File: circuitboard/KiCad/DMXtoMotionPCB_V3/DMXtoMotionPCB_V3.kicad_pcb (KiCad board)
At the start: 2 copper layers, 93.8 x 100 mm, 55 parts, among them J1 12V In, J10 D2, J2 XLR3 IN, J3 XLR3 OUT, J4 D1, J5 INTERFACE, J6 A0, J7 A1, J8 D0, J9 D3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

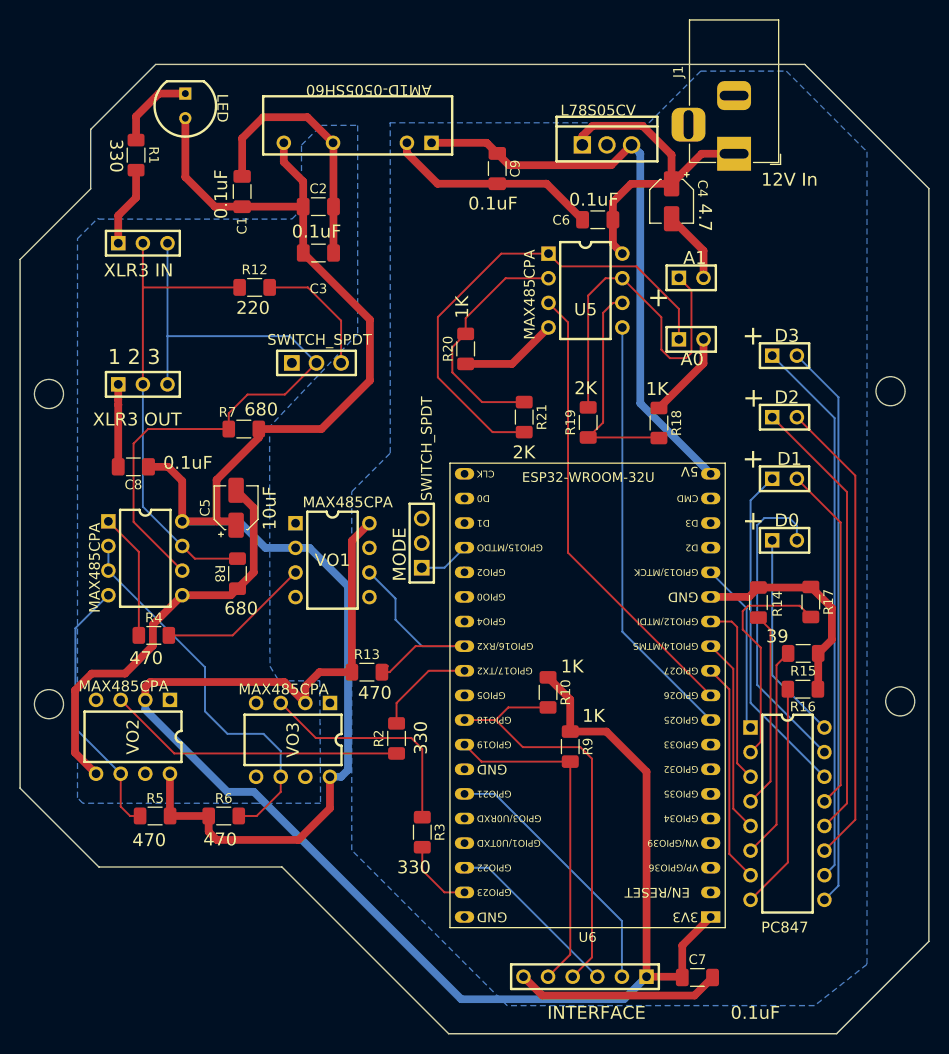
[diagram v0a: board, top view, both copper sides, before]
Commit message: Slight modifications on KiCAD V3 files. Generated fabrication files
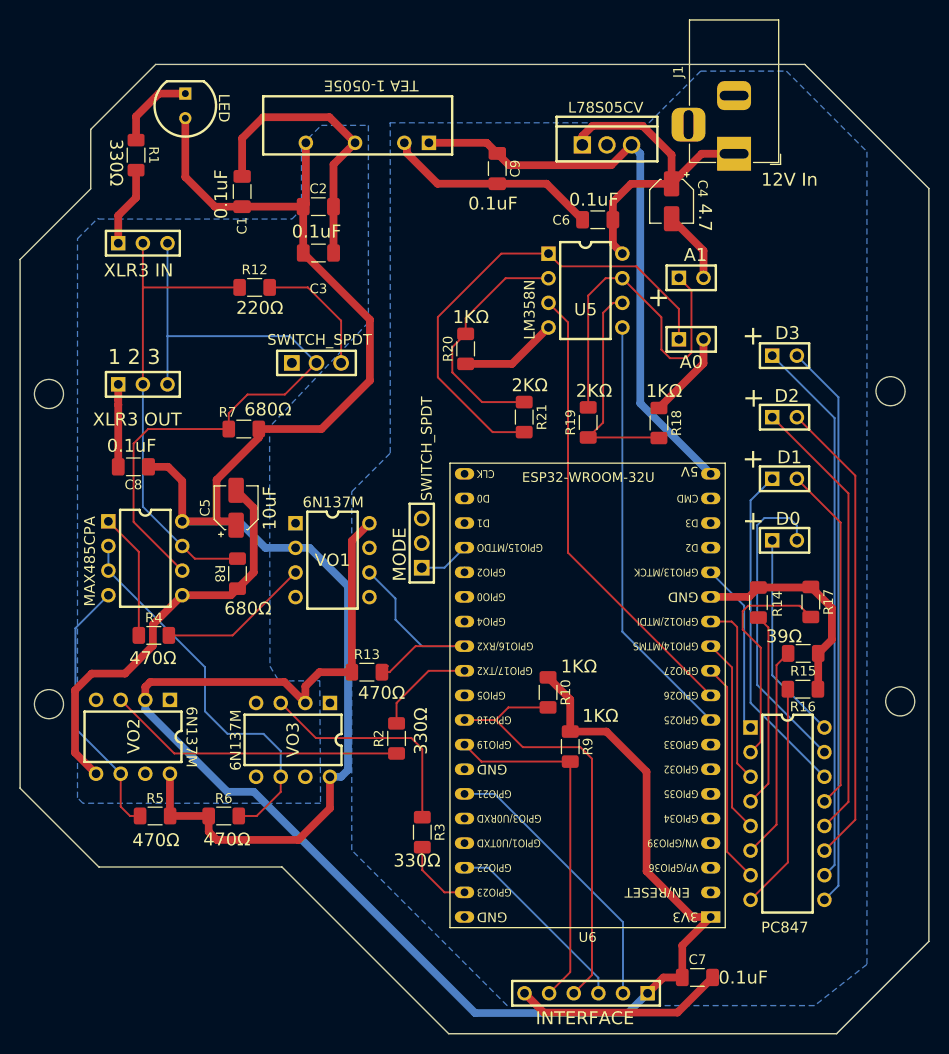
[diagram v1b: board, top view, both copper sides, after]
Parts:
- moved J5 1.71 mm to (158.4, 150.8)
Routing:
- net ISO-GND: track 87.4 -> 90.2 mm
- net Net_33: track 18.4 -> 20.1 mm
- net Net_32: track 27.4 -> 29.2 mm
- net But1: track 44.1 -> 45.7 mm
- net But2: track 35.2 -> 36.9 mm
- net 3.3V_ESP: track 156.7 -> 155.6 mm
- net ISO-5V: track 154.4 -> 153.7 mm
- net GND: track 92.5 -> 93.1 mm
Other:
- board text added: "1KΩ"
- board text added: "220Ω"
- board text added: "2KΩ"
- board text added: "330Ω"
- board text added: "39Ω"
- board text added: "470Ω"
- board text added: "680Ω"
- board text removed: "1K"
- board text removed: "220"
- board text removed: "2K"
- board text removed: "330"
- board text removed: "39"
- board text removed: "470"
- board text removed: "680"

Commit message: Changes of through hole diameters in KiCAD V3 and BOM
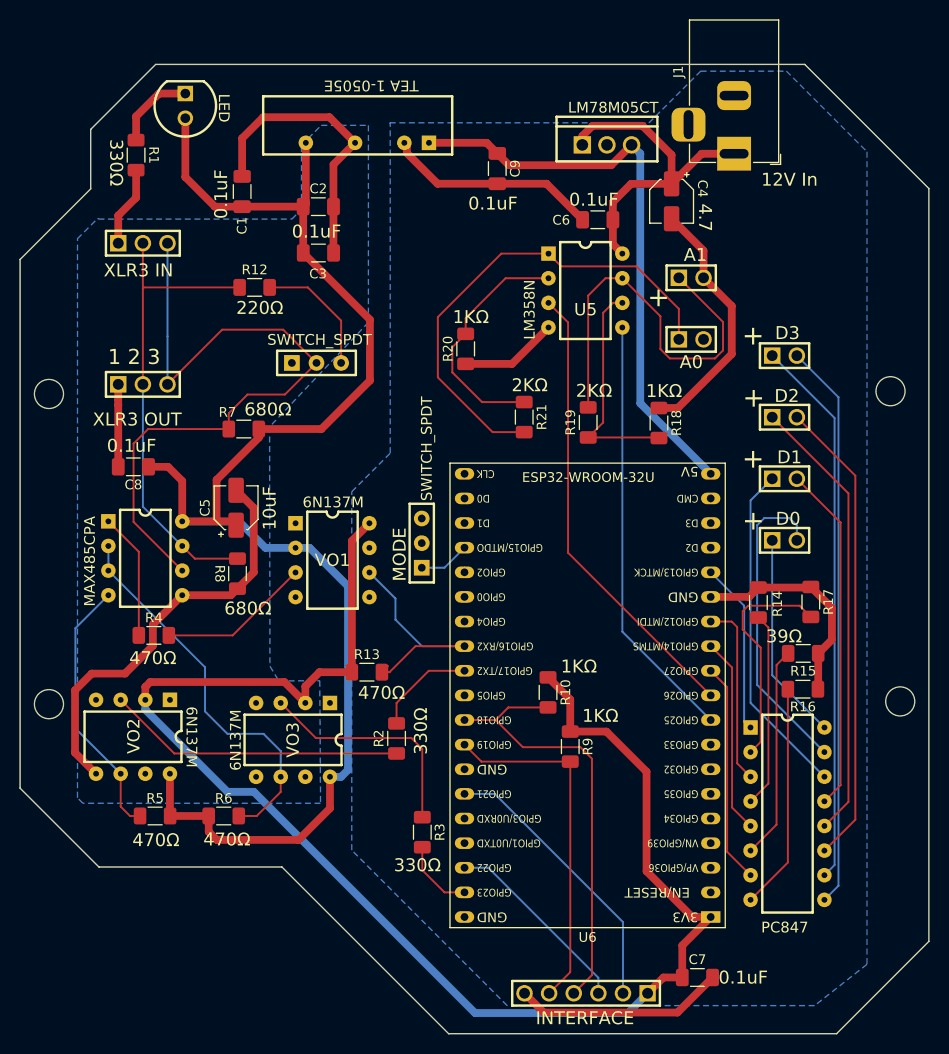
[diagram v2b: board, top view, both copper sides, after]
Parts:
- U4: value L78S05CV -> LM78M05CT
- VO2, VO3: value 6N137M_10 -> 6N137M
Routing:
- net GND: track 93.1 -> 103.0 mm
- net Net_18: track 36.8 -> 41.6 mm
- net Net_17: track 69.5 -> 72.1 mm

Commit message: Actualización de componentes obsoletos
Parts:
- U4: value LM78M05CT -> L78S05CV
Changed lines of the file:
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@@
 			)
 		)
-		(property "Value" "LM78M05CT"
+		(property "Value" "L78S05CV "
 			(at 0 0 0)
 			(layer "F.Fab")
@@
 			(layer "F.SilkS")
 		)
-		(fp_text user "LM78M05CT"
+		(fp_text user "L78S05CV "
 			(at -4.0261 -3.1961 0)
 			(unlocked yes)

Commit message: double checked through holes and part names. Completed BOM
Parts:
- U1: value AM1D-0505SH60 -> TEA 1-0505E
- VO1, VO2, VO3: value 6N137M -> 6N137
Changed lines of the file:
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@@
 			)
 		)
-		(property "Value" "6N137M"
+		(property "Value" "6N137"
 			(at 0 0 0)
 			(layer "F.Fab")
@@
 			(layer "F.SilkS")
 		)
-		(fp_text user "6N137M"
+		(fp_text user "6N137"
 			(at -3.1411 -5.3889 -90)
 			(unlocked yes)
@@
 		)
 		(fp_line
-			(start 0.9 1.9)
+			(start 0.9 2.2352)
 			(end 0.9 4.6)
 			(stroke
@@
 		(fp_line
 			(start 0.9 -4.6)
-			(end 0.9 -2)
+			(end 0.9 -2.2352)
 			(stroke
 				(width 0.12)
@@
 		(pad "1" thru_hole rect
 			(at 0 0 270)
-			(size 3.5 3.5)
-			(drill oval 1 3)
+			(size 3.5 4)
+			(drill oval 1 3.5)
 			(layers "*.Cu" "*.Mask")
 			(remove_unused_layers no)
@@
 		(pad "1" thru_hole rect
 			(at -2.54 0 90)
-			(size 1.62 1.62)
-			(drill 0.8)
+			(size 1.92 1.92)
+			(drill 1.1)
 			(layers "*.Cu" "*.Mask")
 			(remove_unused_layers no)
@@
 		(pad "2" thru_hole circle
 			(at 0 0 90)
-			(size 1.62 1.62)
-			(drill 0.8)
+			(size 1.92 1.92)
+			(drill 1.1)
 			(layers "*.Cu" "*.Mask")
 			(remove_unused_layers no)
@@
 		(pad "3" thru_hole circle
 			(at 2.54 0 90)
-			(size 1.62 1.62)
-			(drill 0.8)
+			(size 1.92 1.92)
+			(drill 1.1)
 			(layers "*.Cu" "*.Mask")
 			(remove_unused_layers no)
@@
 			)
 		)
-		(property "Value" "AM1D-0505SH60"
+		(property "Value" "TEA 1-0505E"
 			(at 0 0 180)
 			(layer "F.Fab")
@@
 			)
 		)
-		(property "Value" "6N137M"
+		(property "Value" "6N137"
 			(at -0.07 0.1 90)
 			(layer "F.Fab")
@@
 			(layer "F.SilkS")
 		)
-		(fp_text user "6N137M"
+		(fp_text user "6N137"
 			(at -3.09 -5.32 0)
 			(unlocked yes)
@@
 		(pad "1" thru_hole rect
 			(at -2.54 0)
-			(size 1.62 1.62)
-			(drill 0.8)
+			(size 1.92 1.92)
+			(drill 1.1)
 			(layers "*.Cu" "*.Mask")
 			(remove_unused_layers no)
@@
 		(pad "2" thru_hole circle
 			(at 0 0)
-			(size 1.62 1.62)
-			(drill 0.8)
+			(size 1.92 1.92)
+			(drill 1.1)
 			(layers "*.Cu" "*.Mask")
 			(remove_unused_layers no)
@@
 		(pad "3" thru_hole circle
 			(at 2.54 0)
-			(size 1.62 1.62)
-			(drill 0.8)
+			(size 1.92 1.92)
+			(drill 1.1)
 			(layers "*.Cu" "*.Mask")
 			(remove_unused_layers no)
@@
 			)
 		)
-		(property "Value" "6N137M"
+		(property "Value" "6N137"
 			(at 0.2414 -0.2489 0)
 			(layer "F.Fab")
@@
 			(layer "F.SilkS")
 		)
-		(fp_text user "6N137M"
+		(fp_text user "6N137"
 			(at 3.1914 5.2611 90)
 			(unlocked yes)

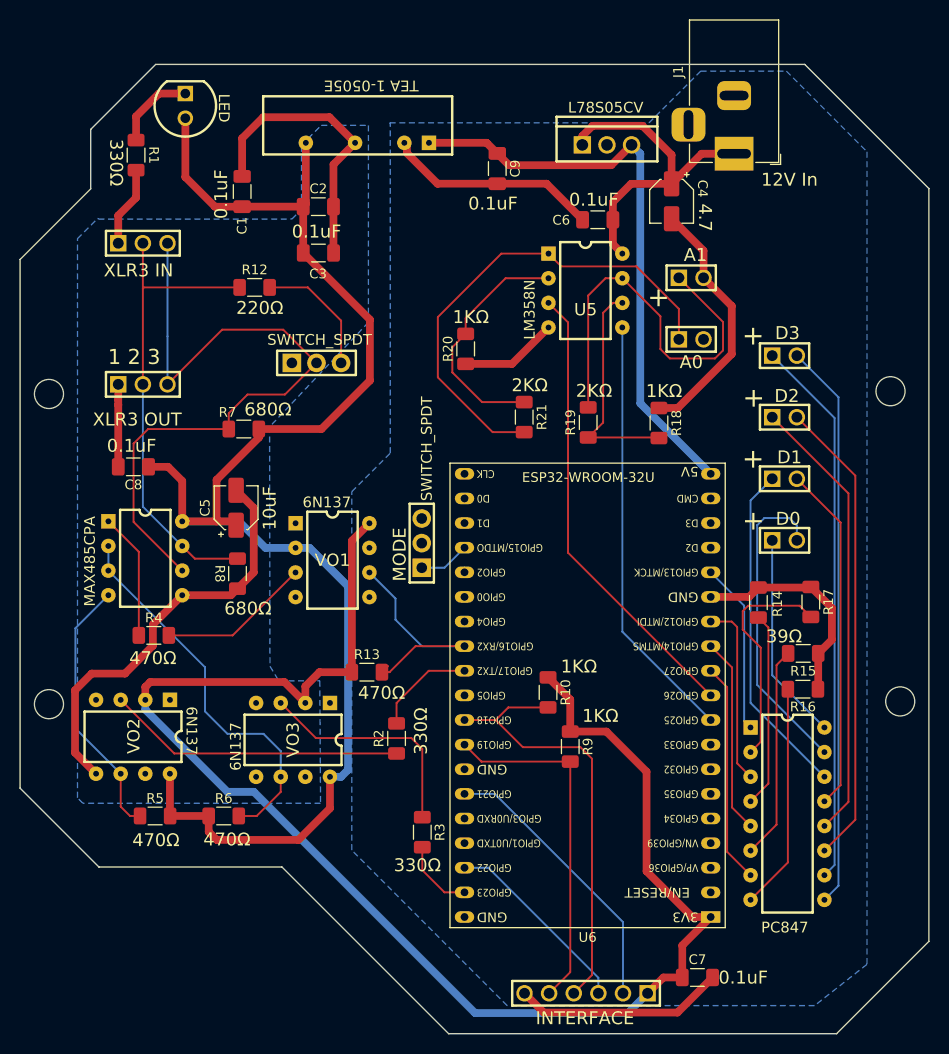
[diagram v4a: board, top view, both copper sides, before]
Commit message: trace adjustments
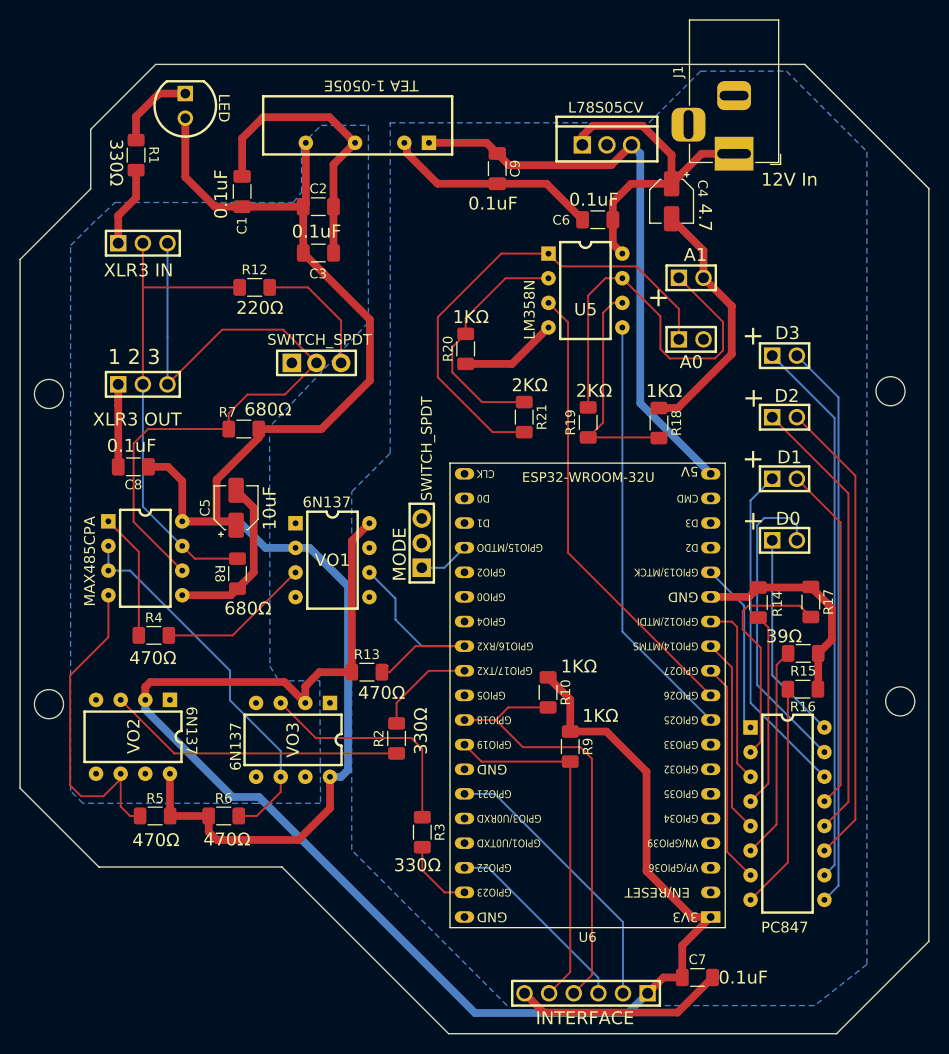
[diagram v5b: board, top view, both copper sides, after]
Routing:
- net ISO-GND: track 90.2 -> 64.3 mm
- net Net_15: track 27.5 -> 34.0 mm
- net Net_14: track 40.3 -> 39.4 mm
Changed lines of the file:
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@@
-	)
-	(segment
-		(start 124.1386 130.0486)
-		(end 146.96 152.87)
-		(width 0.8)
-		(layer "B.Cu")
-		(net 1)
-	)
-	(segment
-		(start 121.4186 130.0486)
-		(end 124.1386 130.0486)
-		(width 0.8)
-		(layer "B.Cu")
-		(net 1)
-	)
-	(segment
-		(start 112.9411 121.5711)
-		(end 121.4186 130.0486)
-		(width 0.8)
-		(layer "B.Cu")
-		(net 1)
 	)
 	(segment
@@
 	)
 	(segment
+		(start 121.95 130.58)
+		(end 124.67 130.58)
+		(width 0.8)
+		(layer "B.Cu")
+		(net 1)
+	)
+	(segment
+		(start 162.72 152.87)
+		(end 164.76 150.83)
+		(width 0.8)
+		(layer "B.Cu")
+		(net 1)
+	)
+	(segment
+		(start 124.67 130.58)
+		(end 146.96 152.87)
+		(width 0.8)
+		(layer "B.Cu")
+		(net 1)
+	)
+	(segment
+		(start 112.9411 121.5711)
+		(end 121.95 130.58)
+		(width 0.8)
+		(layer "B.Cu")
+		(net 1)
+	)
+	(segment
 		(start 146.96 152.87)
 		(end 162.72 152.87)
@@
 	)
 	(segment
-		(start 162.72 152.87)
-		(end 164.76 150.83)
-		(width 0.8)
-		(layer "B.Cu")
-		(net 1)
-	)
-	(segment
 		(start 150.4625 65.4)
 		(end 161.0122 65.4)
@@
 	)
 	(segment
-		(start 105.69 126.01)
-		(end 107.8611 128.1811)
-		(width 0.8)
-		(layer "F.Cu")
-		(net 7)
-	)
-	(segment
 		(start 110.15 73.45)
 		(end 110.15 70.59)
@@
 	)
 	(segment
-		(start 105.69 119.574141)
-		(end 105.69 126.01)
-		(width 0.8)
-		(layer "F.Cu")
-		(net 7)
-	)
-	(segment
 		(start 132.3525 69.68)
 		(end 132.3525 65.3237)
@@
 	)
 	(segment
-		(start 113.72 112.7972)
-		(end 113.72 114.976852)
-		(width 0.8)
-		(layer "F.Cu")
-		(net 7)
-	)
-	(segment
 		(start 132.3525 69.68)
 		(end 132.3525 74.45)
@@
 	)
 	(segment
-		(start 113.72 114.976852)
-		(end 110.846852 117.85)
-		(width 0.8)
-		(layer "F.Cu")
-		(net 7)
-	)
-	(segment
 		(start 124.12498 107.415048)
 		(end 122.450028 109.09)
@@
 	)
 	(segment
-		(start 116.7511 109.7661)
-		(end 113.72 112.7972)
-		(width 0.8)
-		(layer "F.Cu")
-		(net 7)
-	)
-	(segment
-		(start 107.414141 117.85)
-		(end 105.69 119.574141)
-		(width 0.8)
-		(layer "F.Cu")
-		(net 7)
-	)
-	(segment
-		(start 110.846852 117.85)
-		(end 107.414141 117.85)
-		(width 0.8)
-		(layer "F.Cu")
-		(net 7)
-	)
-	(segment
 		(start 110.15 70.59)
 		(end 111.98864 68.75136)
@@
 	)
 	(segment
-		(start 119.1 121.75)
-		(end 121.41 124.06)
+		(start 121.68 117.54)
+		(end 121.68 120.61)
 		(width 0.2)
 		(layer "B.Cu")
@@
 	)
 	(segment
-		(start 119.1 117.195)
-		(end 119.1 121.75)
+		(start 109.1311 107.2261)
+		(end 111.3661 107.2261)
 		(width 0.2)
 		(layer "B.Cu")
@@
 	)
 	(segment
-		(start 121.41 124.06)
-		(end 125.13 124.06)
-		(width 0.2)
-		(layer "B.Cu")
-		(net 44)
-	)
-	(segment
-		(start 109.1311 107.2261)
-		(end 119.1 117.195)
+		(start 121.68 120.61)
+		(end 126.9111 125.8411)
 		(width 0.2)
 		(layer "B.Cu")
@@
 	)
 	(segment
-		(start 125.13 124.06)
-		(end 126.9111 125.8411)
+		(start 111.3661 107.2261)
+		(end 121.68 117.54)
 		(width 0.2)
 		(layer "B.Cu")
@@
 	)
 	(segment
+		(start 105.18 118.04)
+		(end 105.18 129.37)
+		(width 0.2)
+		(layer "F.Cu")
+		(net 46)
+	)
+	(segment
+		(start 109.1311 114.0889)
+		(end 105.18 118.04)
+		(width 0.2)
+		(layer "F.Cu")
+		(net 46)
+	)
+	(segment
+		(start 108.62 130.5)
+		(end 110.4011 128.7189)
+		(width 0.2)
+		(layer "F.Cu")
+		(net 46)
+	)
+	(segment
+		(start 105.18 129.37)
+		(end 106.31 130.5)
+		(width 0.2)
+		(layer "F.Cu")
+		(net 46)
+	)
+	(segment
+		(start 106.31 130.5)
+		(end 108.62 130.5)
+		(width 0.2)
+		(layer "F.Cu")
+		(net 46)
+	)
+	(segment
 		(start 110.4011 131.5711)
 		(end 110.4011 128.1811)
@@
 	)
 	(segment
+		(start 109.1311 109.7661)
+		(end 109.1311 114.0889)
+		(width 0.2)
+		(layer "F.Cu")
+		(net 46)
+	)
+	(segment
 		(start 111.37 132.54)
 		(end 110.4011 131.5711)
@@
 	)
 	(segment
-		(start 110.4011 128.1811)
-		(end 105.73 123.51)
-		(width 0.2)
-		(layer "B.Cu")
-		(net 46)
-	)
-	(segment
-		(start 105.73 113.1672)
-		(end 109.1311 109.7661)
-		(width 0.2)
-		(layer "B.Cu")
-		(net 46)
-	)
-	(segment
-		(start 105.73 123.51)
-		(end 105.73 113.1672)
-		(width 0.2)
-		(layer "B.Cu")
+		(start 110.4011 128.7189)
+		(end 110.4011 128.1811)
+		(width 0.2)
+		(layer "F.Cu")
 		(net 46)
 	)
@@
 		(polygon
 			(pts
-				(xy 108.1 70.96) (xy 128.06 70.96) (xy 129.05 69.97) (xy 129.05 63.34) (xy 131.0964 61.2936) (xy 135.9586 61.2936)
+				(xy 109.81 69.25) (xy 128.21 69.25) (xy 129.05 68.22) (xy 129.05 63.34) (xy 131.0964 61.2936) (xy 135.9586 61.2936)
 				(xy 135.9586 81.616903) (xy 125.759939 92.398216) (xy 125.801564 117.09) (xy 126.717958 118.61)
-				(xy 130.94 118.59) (xy 131.02 131.23) (xy 124.5 131.23) (xy 106.51 131.23) (xy 105.94 130.66) (xy 105.94 72.99)
+				(xy 130.94 118.59) (xy 131.02 131.23) (xy 124.5 131.23) (xy 106.51 131.23) (xy 105.23 129.95) (xy 105.23 73.7)
 				(xy 108.06 70.87) (xy 108.06 70.92)
 			)
